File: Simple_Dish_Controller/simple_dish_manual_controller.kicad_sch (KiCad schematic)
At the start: 7 parts, among them J1 Screw_Terminal_01x02, SW1 SW_SPST, U1 AMS1117-5.0

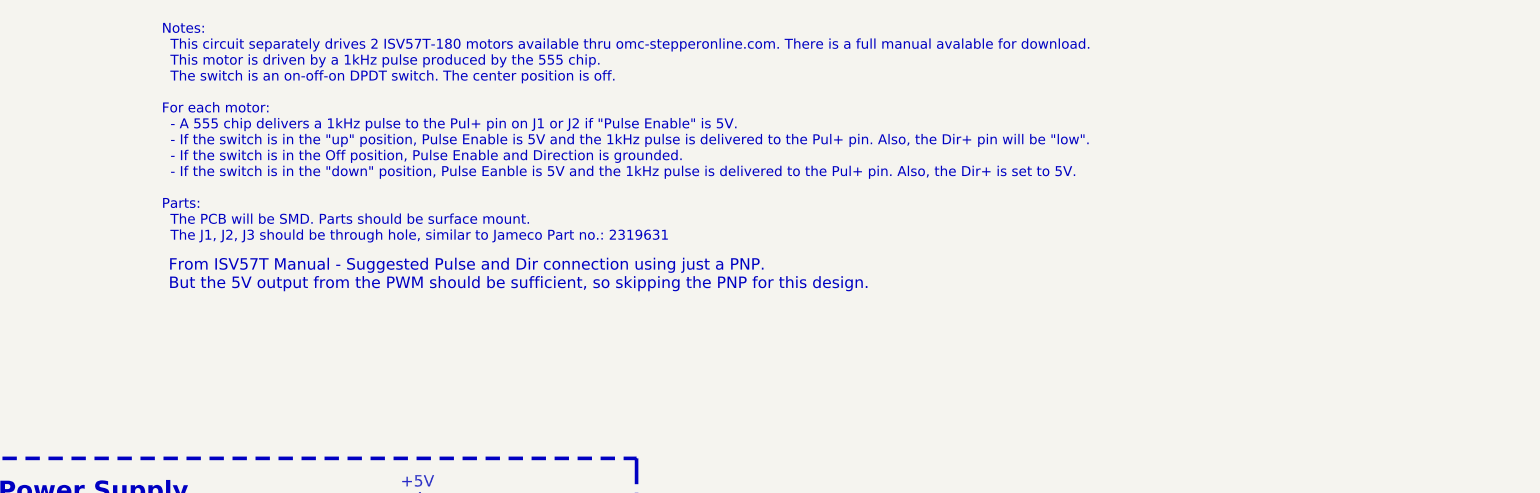
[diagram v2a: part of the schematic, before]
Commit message: Footprints defined - passes ERC
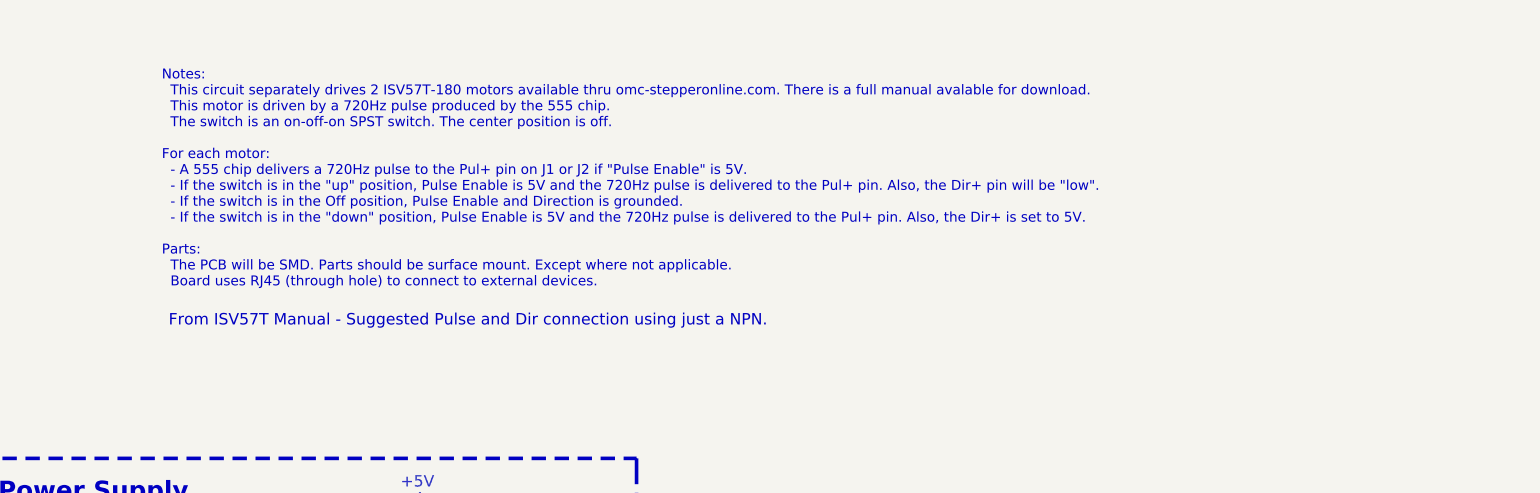
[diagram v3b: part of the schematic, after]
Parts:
- removed C2: 22uF, GRM219R61C226ME15K:CAPC2012X100N, symbol GRM219R61C226ME15K:GRM219R61C226ME15K
- added C2: 22uF, Cap_SMD_22uF_0805:CAPC2012X100N, symbol Cap_SMD_22uF_0805:GRM219R61C226ME15K
- C1: footprint GRM219R61C226ME15K:CAPC2012X100N -> Cap_SMD_22uF_0805:CAPC2012X100N
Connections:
- net +5V: now also C2.2
- net GND: now also C2.1
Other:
- note added: "From ISV57T Manual - Suggested Pulse and Dir connection using just a NPN."
- note added: "Notes: This circuit separately drives 2 ISV57T-180 motors available thru omc-stepperonline.com. There is a full manual avalable for download. This motor is driven by a 720Hz pulse produced by the 555 chip. The switch is an on-off-on SPST switch. The center position is off. For each motor: - A 555 chip delivers a 720Hz pulse to the Pul+ pin on J1 or J2 if "Pulse Enable" is 5V. - If the switch is i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"
- note removed: "From ISV57T Manual - Suggested Pulse and Dir connection using just a PNP. But the 5V output from the PWM should be sufficient, so skipping the PNP for this design."
- note removed: "Notes: This circuit separately drives 2 ISV57T-180 motors available thru omc-stepperonline.com. There is a full manual avalable for download. This motor is driven by a 1kHz pulse produced by the 555 chip. The switch is an on-off-on DPDT switch. The center position is off. For each motor: - A 555 chip delivers a 1kHz pulse to the Pul+ pin on J1 or J2 if "Pulse Enable" is 5V. - If the switch is in 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"
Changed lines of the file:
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@@
 		)
 	)
-	(text "Notes:\n  This circuit separately drives 2 ISV57T-180 motors available thru omc-stepperonline.com. There is a full manual avalable for download.\n  This motor is driven by a 1kHz pulse produced by the 555 chip.\n  The switch is an on-off-on DPDT switch. The center position is off.\n\nFor each motor:\n  - A 555 chip delivers a 1kHz pulse to the Pul+ pin on J1 or J2 if \"Pulse Enable\" is 5V.\n  - If the switch is in the \"up\" position, Pulse Enable is 5V and the 1kHz pulse is delivered to the Pul+ pin. Also, the Dir+ pin will be \"low\".\n  - If the switch is in the Off position, Pulse Enable and Direction is grounded.\n  - If the switch is in the \"down\" position, Pulse Eanble is 5V and the 1kHz pulse is delivered to the Pul+ pin. Also, the Dir+ is set to 5V.\n\nParts:\n  The PCB will be SMD. Parts should be surface mount.\n  The J1, J2, J3 should be through hole, similar to Jameco Part no.: 2319631\n"
+	(text "Notes:\n  This circuit separately drives 2 ISV57T-180 motors available thru omc-stepperonline.com. There is a full manual avalable for download.\n  This motor is driven by a 720Hz pulse produced by the 555 chip.\n  The switch is an on-off-on SPST switch. The center position is off.\n\nFor each motor:\n  - A 555 chip delivers a 720Hz pulse to the Pul+ pin on J1 or J2 if \"Pulse Enable\" is 5V.\n  - If the switch is in the \"up\" position, Pulse Enable is 5V and the 720Hz pulse is delivered to the Pul+ pin. Also, the Dir+ pin will be \"low\".\n  - If the switch is in the Off position, Pulse Enable and Direction is grounded.\n  - If the switch is in the \"down\" position, Pulse Enable is 5V and the 720Hz pulse is delivered to the Pul+ pin. Also, the Dir+ is set to 5V.\n\nParts:\n  The PCB will be SMD. Parts should be surface mount. Except where not applicable.\n  Board uses RJ45 (through hole) to connect to external devices."
 		(exclude_from_sim no)
-		(at 159.258 13.97 0)
+		(at 159.258 19.05 0)
 		(effects
 			(font
@@
 		)
 	)
-	(text "From ISV57T Manual - Suggested Pulse and Dir connection using just a PNP.\nBut the 5V output from the PWM should be sufficient, so skipping the PNP for this design."
+	(text "From ISV57T Manual - Suggested Pulse and Dir connection using just a NPN.\n"
 		(exclude_from_sim no)
-		(at 160.02 41.91 0)
+		(at 160.02 46.99 0)
 		(effects
 			(font
@@
 	)
 	(image
-		(at 262.89 42.5387)
+		(at 262.89 47.6187)
 		(scale 0.220951)
 		(data "iVBORw0KGgoAAAANSUhEUgAAAaUAAAEOCAIAAACma5/UAAAAA3NCSVQICAjb4U/gAAAACXBIWXMA"
@@
 			"AAAAAAAAAAAAAAAAAAAAAAAAAAAAAAAAAAAAAAAAAAAAAAAAAAAAAAAAAAAAAAAAAAAAAAAAAAAA"
 			"AAAAAAAAAAAAAAAAAAAAAAAAAAAAAAAAAAAAAAAAAAAAAAAAAAAAAAAAAAAAAAAAAAAAAAAAAAAA"
+			"AAAAAAAAAAAAAAAAAAAAAAAAAAAAAAAAAAAAAAAAAAAAAAAAAAAAAAAAAAAAAAAAAAAAAAAAAAAA"
+			"AAAAAAAAAAAAAAAAAAAAAAAAAAAAAAAAAAAAAAAAAAAAAAAAAAAAAAAAAAAAAAAAAAAAAAAAAAAA"
+			"AAAAAAAAAAAAAAAAAAAAAAAAAAAAAAAAAAAAAAAAAAAAAAAAAAAAAAAAAAAAAAAAAAAAAAAAAAAA"
+			"AAAAAAAAAAAAAAAAAAAAAAAAAAAAAAAAAAAAAAAAAAAAAAAAAAAAAAAAAAAAAAAAAAAAAAAAAAAA"
+			"AAAAAAAAAAAAAAAAAAAAAAAAAAAAAAAAAAAAAAAAAAAAAAAAAAAAAAAAAAAAAAAAAAAAAAAAAAAA"
+			"AAAAAAAAAAAAAAAAAAAAAAAAAAAAAAAAAAAAAAAAAAAAAAAAAAAAAAAAAAAAAAAAAAAAAAAAAAAA"
+			"AAAAAAAAAAAAAAAAAAAAAAAAAAAAAAAAAAAAAAAAAAAAAAAAAAAAAAAAAAAAAAAAAAAAAAAAAAAA"
+			"AAAAAAAAAAAAAAAAAAAAAAAAAAAAAAAAAAAAAAAAAAAAAAAAAAAAAAAAAAAAAAAAAAAAAAAAAAAA"
+			"AAAAAAAAAAAAAAAAAAAAAAAAAAAAAAAAAAAAAAAAAAAAAAAAAAAAAAAAAAAAAAAAAAAAAAAAAAAA"
+			"AAAAAAAAAAAAAAAAAAAAAAAAAAAAAAAAAAAAAAAAAAAAAAAAAAAAAAAAAAAAAAAAAAAAAAAAAAAA"
+			"AAAAAAAAAAAAAAAAAAAAAAAAAAAAAAAAAAAAAAAAAAAAAAAAAAAAAAAAAAAAAAAAAAAAAAAAAAAA"
+			"AAAAAAAAAAAAAAAAAAAAAAAAAAAAAAAAAAAAAAAAAAAAAAAAAAAAAAAAAAAAAAAAAAAAAAAAAAAA"
+			"AAAAAAAAAAAAAAAAAAAAAAAAAAAAAAAAAAAAAAAAAAAAAAAAAAAAAAAAAAAAAAAAAAAAAAAAAAAA"
+			"AAAAAAAAAAAAAAAAAAAAAAAAAAAAAAAAAAAAAAAAAAAAAAAAAAAAAAAAAAAAAAAAAAAAAAAAAAAA"
+			"AAAAAAAAAAAAAAAAAAAAAAAAAAAAAAAAAAAAAAAAAAAAAAAAAAAAAAAAAAAAAAAAAAAAAAAAAAAA"
+			"AAAAAAAAAAAAAAAAAAAAAAAAAAAAAAAAAAAAAAAAAAAAAAAAAAAAAAAAAAAAAAAAAAAAAAAAAAAA"
+			"AAAAAAAAAAAAAAAAAAAAAAAAAAAAAAAAAAAAAAAAAAAAAAAAAAAAAAAAAAAAAAAAAAAAAAAAAAAA"
+			"AAAAAAAAAAAAAAAAAAAAAAAAAAAAAAAAAAAAAAAAAAAAAAAAAAAAAAAAAAAAAAAAAAAAAAAAAAAA"
 			"AAAAAAAAAAAAAAAAAAAAAAAAAAAAAAAAAAAAAA=="
 		)
@@
 				(path "/8648ccd3-30ce-4b98-baff-aeab56a7c9f5"
 					(reference "#PWR03")
-					(unit 1)
-				)
-			)
-		)
-	)
-	(symbol
-		(lib_id "GRM219R61C226ME15K:GRM219R61C226ME15K")
-		(at 187.96 88.9 90)
-		(unit 1)
-		(exclude_from_sim no)
-		(in_bom yes)
-		(on_board yes)
-		(dnp no)
-		(property "Reference" "C2"
-			(at 190.5 86.36 90)
-			(effects
-				(font
-					(size 1.27 1.27)
-				)
-				(justify right)
-			)
-		)
-		(property "Value" "22uF"
-			(at 190.5 88.9 90)
-			(effects
-				(font
-					(size 1.27 1.27)
-				)
-				(justify right)
-			)
-		)
-		(property "Footprint" "GRM219R61C226ME15K:CAPC2012X100N"
-			(at 187.96 88.9 0)
-			(effects
-				(font
-					(size 1.27 1.27)
-				)
-				(justify bottom)
-				(hide yes)
-			)
-		)
-		(property "Datasheet" ""
-			(at 187.96 88.9 0)
-			(effects
-				(font
-					(size 1.27 1.27)
-				)
-				(hide yes)
-			)
-		)
-		(property "Description" ""
-			(at 187.96 88.9 0)
-			(effects
-				(font
-					(size 1.27 1.27)
-				)
-				(hide yes)
-			)
-		)
-		(property "MF" "Murata"
-			(at 187.96 88.9 0)
-			(effects
-				(font
-					(size 1.27 1.27)
-				)
-				(justify bottom)
-				(hide yes)
-			)
-		)
-		(property "Description_1" "SMD Capacitor X5R(EIA) with Capacitance: 22uF Tol. 20%. Rated Voltage: 16Vdc"
-			(at 187.96 88.9 0)
-			(effects
-				(font
-					(size 1.27 1.27)
-				)
-				(justify bottom)
-				(hide yes)
-			)
-		)
-		(property "Package" "805-2 Murata"
-			(at 187.96 88.9 0)
-			(effects
-				(font
-					(size 1.27 1.27)
-				)
-				(justify bottom)
-				(hide yes)
-			)
-		)
-		(property "Price" "None"
-			(at 187.96 88.9 0)
-			(effects
-				(font
-					(size 1.27 1.27)
-				)
-				(justify bottom)
-				(hide yes)
-			)
-		)
-		(property "SnapEDA_Link" "https://www.snapeda.com/parts/GRM219R61C226ME15K/Murata/view-part/?ref=snap"
-			(at 187.96 88.9 0)
-			(effects
-				(font
-					(size 1.27 1.27)
-				)
-				(justify bottom)
-				(hide yes)
-			)
-		)
-		(property "MP" "GRM219R61C226ME15K"
-			(at 187.96 88.9 0)
-			(effects
-				(font
-					(size 1.27 1.27)
-				)
-				(justify bottom)
-				(hide yes)
-			)
-		)
-		(property "Availability" "In Stock"
-			(at 187.96 88.9 0)
-			(effects
-				(font
-					(size 1.27 1.27)
-				)
-				(justify bottom)
-				(hide yes)
-			)
-		)
-		(property "Check_prices" "https://www.snapeda.com/parts/GRM219R61C226ME15K/Murata/view-part/?ref=eda"
-			(at 187.96 88.9 0)
-			(effects
-				(font
-					(size 1.27 1.27)
-				)
-				(justify bottom)
-				(hide yes)
-			)
-		)
-		(pin "2"
-		)
-		(pin "1"
-		)
-		(instances
-			(project "simple_dish_manual_controller"
-				(path "/8648ccd3-30ce-4b98-baff-aeab56a7c9f5"
-					(reference "C2")
 					(unit 1)
 				)
@@
 	)
 	(symbol
+		(lib_id "Cap_SMD_22uF_0805:GRM219R61C226ME15K")
+		(at 187.96 88.9 90)
+		(unit 1)
+		(exclude_from_sim no)
+		(in_bom yes)
+		(on_board yes)
+		(dnp no)
+		(property "Reference" "C2"
+			(at 190.5 86.36 90)
+			(effects
+				(font
+					(size 1.27 1.27)
+				)
+				(justify right)
+			)
+		)
+		(property "Value" "22uF"
+			(at 190.5 88.9 90)
+			(effects
+				(font
+					(size 1.27 1.27)
+				)
+				(justify right)
+			)
+		)
+		(property "Footprint" "Cap_SMD_22uF_0805:CAPC2012X100N"
+			(at 187.96 88.9 0)
+			(effects
+				(font
+					(size 1.27 1.27)
+				)
+				(justify bottom)
+				(hide yes)
+			)
+		)
+		(property "Datasheet" ""
+			(at 187.96 88.9 0)
+			(effects
+				(font
+					(size 1.27 1.27)
+				)
+				(hide yes)
+			)
+		)
+		(property "Description" ""
+			(at 187.96 88.9 0)
+			(effects
+				(font
+					(size 1.27 1.27)
+				)
+				(hide yes)
+			)
+		)
+		(property "MF" "Murata"
+			(at 187.96 88.9 0)
+			(effects
+				(font
+					(size 1.27 1.27)
+				)
+				(justify bottom)
+				(hide yes)
+			)
+		)
+		(property "Description_1" "SMD Capacitor X5R(EIA) with Capacitance: 22uF Tol. 20%. Rated Voltage: 16Vdc"
+			(at 187.96 88.9 0)
+			(effects
+				(font
+					(size 1.27 1.27)
+				)
+				(justify bottom)
+				(hide yes)
+			)
+		)
+		(property "Package" "805-2 Murata"
+			(at 187.96 88.9 0)
+			(effects
+				(font
+					(size 1.27 1.27)
+				)
+				(justify bottom)
+				(hide yes)
+			)
+		)
+		(property "Price" "None"
+			(at 187.96 88.9 0)
+			(effects
+				(font
+					(size 1.27 1.27)
+				)
+				(justify bottom)
+				(hide yes)
+			)
+		)
+		(property "SnapEDA_Link" "https://www.snapeda.com/parts/GRM219R61C226ME15K/Murata/view-part/?ref=snap"
+			(at 187.96 88.9 0)
+			(effects
+				(font
+					(size 1.27 1.27)
+				)
+				(justify bottom)
+				(hide yes)
+			)
+		)
+		(property "MP" "GRM219R61C226ME15K"
+			(at 187.96 88.9 0)
+			(effects
+				(font
+					(size 1.27 1.27)
+				)
+				(justify bottom)
+				(hide yes)
+			)
+		)
+		(property "Availability" "In Stock"
+			(at 187.96 88.9 0)
+			(effects
+				(font
+					(size 1.27 1.27)
+				)
+				(justify bottom)
+				(hide yes)
+			)
+		)
+		(property "Check_prices" "https://www.snapeda.com/parts/GRM219R61C226ME15K/Murata/view-part/?ref=eda"
+			(at 187.96 88.9 0)
+			(effects
+				(font
+					(size 1.27 1.27)
+				)
+				(justify bottom)
+				(hide yes)
+			)
+		)
+		(pin "2"
+		)
+		(pin "1"
+		)
+		(instances
+			(project "simple_dish_manual_controller"
+				(path "/8648ccd3-30ce-4b98-baff-aeab56a7c9f5"
+					(reference "C2")
+					(unit 1)
+				)
+			)
+		)
+	)
+	(symbol
 		(lib_id "Regulator_Linear:AMS1117-5.0")
 		(at 175.26 81.28 0)
@@
 			)
 		)
-		(property "Footprint" "GRM219R61C226ME15K:CAPC2012X100N"
+		(property "Footprint" "Cap_SMD_22uF_0805:CAPC2012X100N"
 			(at 162.56 88.9 0)
 			(effects

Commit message: Still creating parts libraries
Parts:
- removed C1, C2: 22uF, Cap_SMD_22uF_0805:CAPC2012X100N, symbol Cap_SMD_22uF_0805:GRM219R61C226ME15K
- removed J1: Screw_Terminal_01x02, TerminalBlock_Phoenix:TerminalBlock_Phoenix_MPT-0,5-2-2.54_1x02_P2.54mm_Horizontal, symbol Connector:Screw_Terminal_01x02
- removed R1: 1k5, Resistor_SMD:R_0201_0603Metric, symbol Device:R
- removed SW1: SW_SPST, symbol Switch:SW_SPST
- removed U1: AMS1117-5.0, Package_TO_SOT_SMD:SOT-223-3_TabPin2, symbol Regulator_Linear:AMS1117-5.0
- added C1, C2: 22uF, DishFootprints:CAP 22uF 0805, symbol DishSymbols:CAP 22uF 0805
- added J1: Screw_Terminal_01x02, DishFootprints:TerminalBlock_Phoenix_MKDS-1,5-2-5.08_1x02_P5.08mm_Horizontal, symbol DishSymbols:Screw_Terminal_01x02
- added J2: Conn_01x02_Pin, DishFootprints:PinHeader_1x02_P2.54mm_Vertical, symbol DishSymbols:Conn_01x02_Pin
- added R1: 1k5, DishFootprints:R_0805, symbol DishSymbols:RES 1.5k 0805
- added U1: AMS1117-5.0, DishFootprints:SOT-223-3_TabPin2, symbol DishSymbols:AMS1117-5.0
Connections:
- net +5V: now also C2.2, U1.2 (VO)
- net GND: now also C1.1, C2.1, J1.2 (Pin_2), R1.2, U1.1 (GND)
- net IN_5VDC: now also J1.1 (Pin_1), J2.2
- net IN_5VDC_SWITCH: now also C1.2, J2.1, U1.3 (VI)
- net at D1.1 (K): now also R1.1
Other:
- note added: "Power Switch"
- note added: "SPST"

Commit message: Latest update
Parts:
- added J10: Screw Terminal 4 pins to board, DishFootprintsSupplier:TERM_SCREW_01x04_VERTICAL_KEYSTONE_7690, symbol DishSymbolsSupplier:Screw Terminal Ground Chassis Vertical
- added U2: 74LS08, DishFootprints:SOIC-14_3.9x8.7mm_P1.27mm, symbol DishSymbols:74LS08
- added U3: 74LS32, DishFootprints:SOIC-14_3.9x8.7mm_P1.27mm, symbol DishSymbols:74LS32
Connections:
- net +5V: now also U2.14 (VCC), U3.14 (VCC)
- net GND: now also U2.7 (GND), U3.7 (GND)
- new net Shield: J10.1_1 (1), J10.1_2 (1__1), J10.1_3 (1__2), J10.1_4 (1__3)
- no-connect marks 0 -> 6
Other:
- note added: "Connect to Chassis"
- note added: "For RJ45 Shielding"
- note added: "Logic Chips Power and Gnd"
- note added: "Shield to Chassis"
- note added: "Unused from Quad OR chip"

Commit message: Updates
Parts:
- removed C1, C2: 22uF, DishFootprints:CAP 22uF 0805, symbol DishSymbols:CAP 22uF 0805
- removed J1: Screw_Terminal_01x02, DishFootprints:TerminalBlock_Phoenix_MKDS-1,5-2-5.08_1x02_P5.08mm_Horizontal, symbol DishSymbols:Screw_Terminal_01x02
- removed J10: Screw Terminal 4 pins to board, DishFootprintsSupplier:TERM_SCREW_01x04_VERTICAL_KEYSTONE_7690, symbol DishSymbolsSupplier:Screw Terminal Ground Chassis Vertical
- removed J2: Conn_01x02_Pin, DishFootprints:PinHeader_1x02_P2.54mm_Vertical, symbol DishSymbols:Conn_01x02_Pin
- removed R1: 1k5, DishFootprints:R_0805, symbol DishSymbols:RES 1.5k 0805
- removed U1: AMS1117-5.0, DishFootprints:SOT-223-3_TabPin2, symbol DishSymbols:AMS1117-5.0
- removed U2: 74LS08, DishFootprints:SOIC-14_3.9x8.7mm_P1.27mm, symbol DishSymbols:74LS08
- removed U3: 74LS32, DishFootprints:SOIC-14_3.9x8.7mm_P1.27mm, symbol DishSymbols:74LS32
- added C1, C2: 22uF, Capacitor_SMD:C_1206_3216Metric, symbol Device:C
- added C3, C4: 0.1uF, Capacitor_SMD:C_1206_3216Metric, symbol Device:C
- added J1: Screw_Terminal_01x02, TerminalBlock_Phoenix:TerminalBlock_Phoenix_MKDS-1,5-2-5.08_1x02_P5.08mm_Horizontal, symbol Connector:Screw_Terminal_01x02
- added J2: Conn_01x02_Pin, Connector_PinHeader_2.54mm:PinHeader_1x02_P2.54mm_Vertical, symbol Connector:Conn_01x02_Pin
- added J3: Screw Terminal To Chassis, DishFootprints:TERM_SCREW_01x04_VERTICAL_KEYSTONE_7690, symbol DishSymbols:Screw Terminal Ground Chassis Vertical
- added R1: 1k, Resistor_SMD:R_0805_2012Metric, symbol Device:R
- added U1: AMS1117-5.0, Package_TO_SOT_SMD:SOT-223-3_TabPin2, symbol Regulator_Linear:AMS1117-5.0
- added U2: 74LS32, Package_SO:SOIC-14_3.9x8.7mm_P1.27mm, symbol 74xx:74LS32
- added U3: 74LS08, Package_SO:SOIC-14_3.9x8.7mm_P1.27mm, symbol 74xx:74LS08
- D1: footprint (none) -> LED_SMD:LED_1206_3216Metric
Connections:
- net +5V: now also C2.1, C3.1, C4.1, U1.2 (VO), U2.14 (VCC), U3.14 (VCC)
- net GND: now also C1.2, C2.2, C3.2, C4.2, J1.2 (Pin_2), R1.2, U1.1 (GND), U2.7 (GND), U3.7 (GND)
- net IN_5VDC: now also J1.1 (Pin_1), J2.2 (Pin_2)
- net IN_5VDC_SWITCH: now also C1.1, J2.1 (Pin_1), U1.3 (VI)
- net Shield: now also J3.1_1 (1), J3.1_2 (1__1), J3.1_3 (1__2), J3.1_4 (1__3)
- net at D1.1 (K): now also R1.1
